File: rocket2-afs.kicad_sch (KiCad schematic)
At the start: 68 parts, among them J1 ARMING_PLUG, J2 POWER, J3 E-MATCH_DROGUE, J4 SWD, J5 E-MATCH_RECOVERY, Q1 Q_NMOS_GSD, Q2 Q_NMOS_GSD, Q3 Q_NMOS_GSD, Q4 Q_NMOS_GSD, Q5 Q_NMOS_GSD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

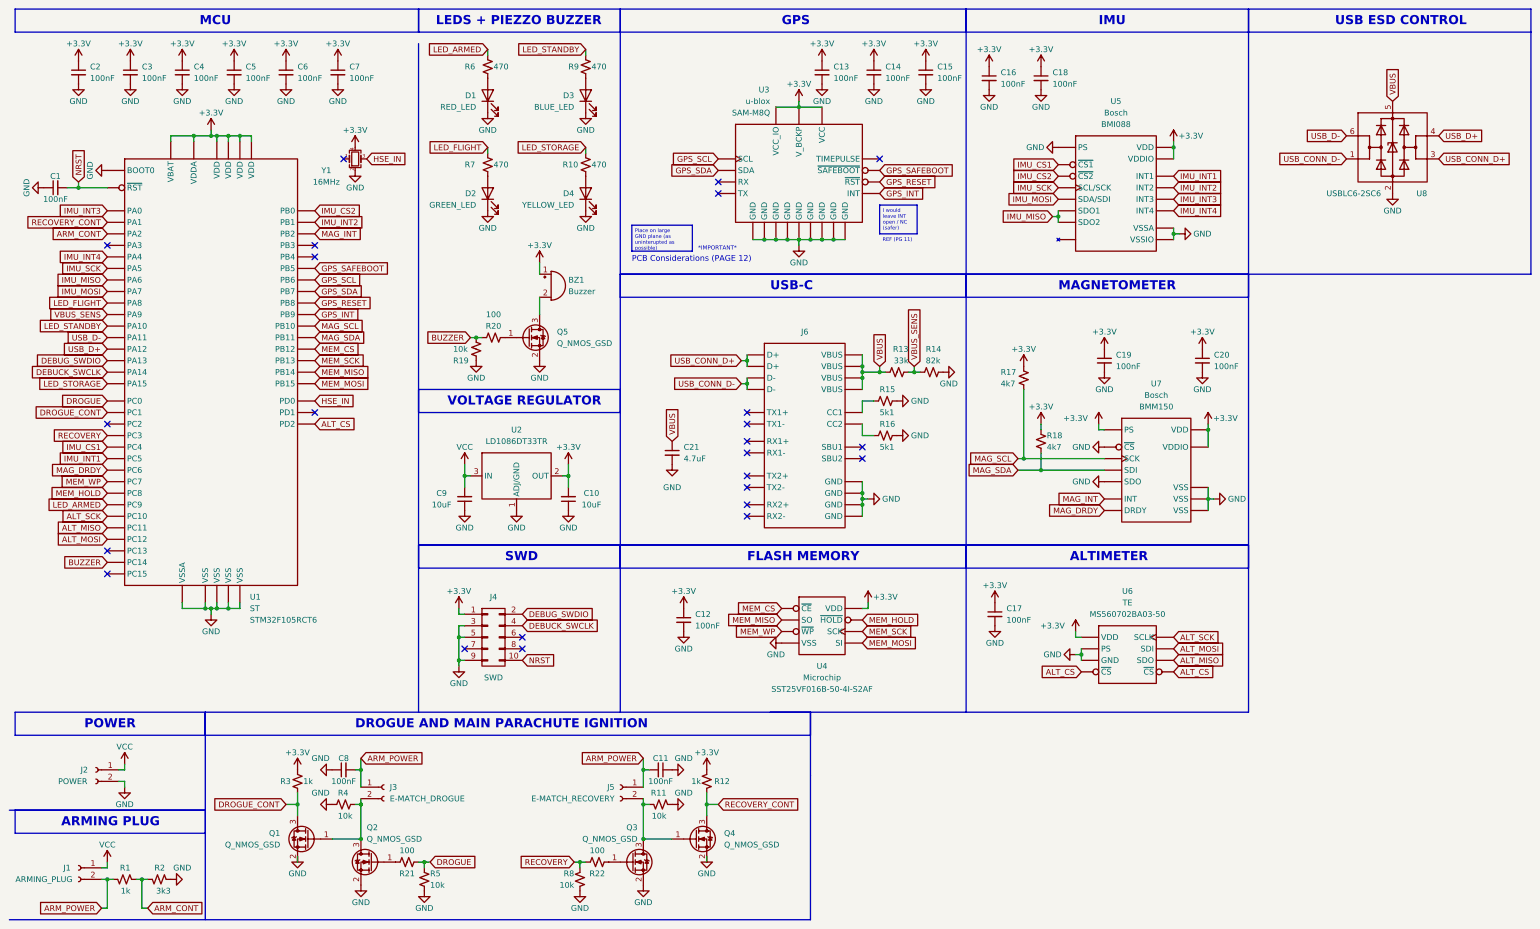
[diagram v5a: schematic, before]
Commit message: Changed Debug Symbol to UCIRP-L Library footrpint
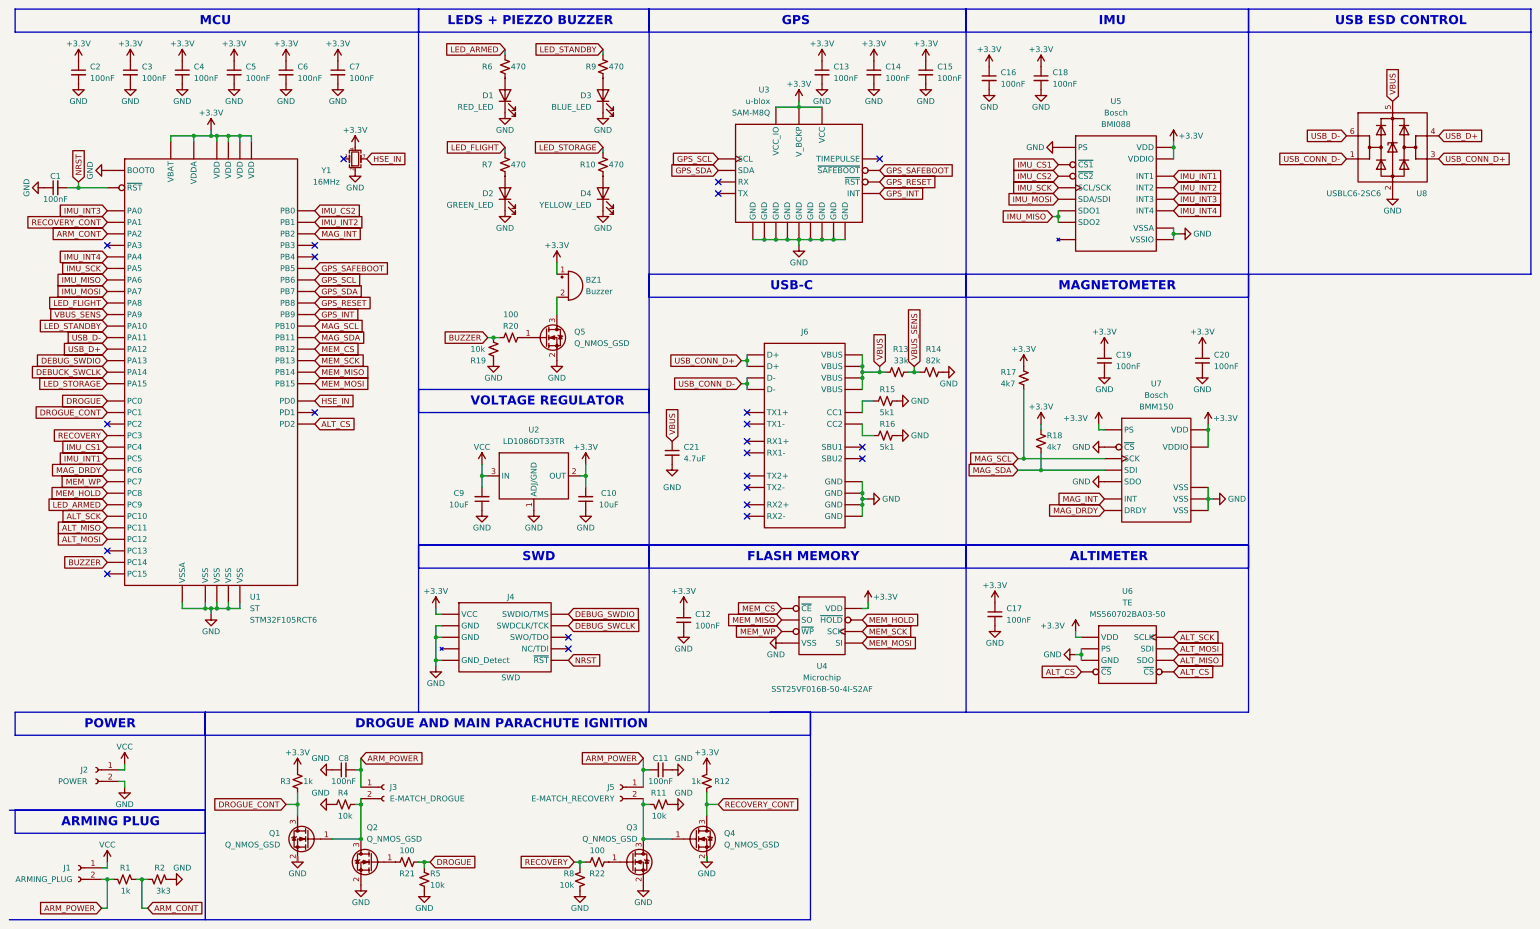
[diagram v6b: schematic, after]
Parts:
- J4: symbol Connector_Generic:Conn_02x05_Odd_Even -> UCIRP-KiCAD-Lib:ARM_Cortex_Debug
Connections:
- net DEBUCK_SWCLK: no longer J4.4 (Pin_4)
- new net DEBUG_SWCLK: J4.4 (SWDCLK/TCK)
- no-connect marks 24 -> 23
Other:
- note removed: "*IMPORTANT*"
- note removed: "PCB Considerations (PAGE 12)"
- note removed: "REF (PG 11)"
- moved on the sheet: BZ1, C10, C9, D1, D2, D3, D4, Q5, R10, R19, R20, R6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

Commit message: Final tweaks
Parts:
- C1, C11, C12, C13, C14, C15, C16, C17, C18, C19, C2, C20, C3, C4, C5, C6, C7, C8: Part # Generic 0603 6.3V 100nF X7R MLCC Capacitor -> Generic 0603 6.3V 100nF X7R MLCC
- C10, C9: Part # Generic 0603 6.3V 10uF X7R MLCC Capacitor -> Generic 0603 6.3V 10uF X7R MLCC
- C21: Part # Generic 0603 6.3V 4.7nF X7R MLCC Capacitor -> Generic 0603 6.3V 4.7uF X7R MLCC
- J4: Part # Generic 2x05 P1.27mm Vertical SMD -> Generic 2x05 P1.27mm Vertical Pin Header SMD
- U4: Manufacturer Microchip -> Winbond; Part # SST25VF016B-50-4I-S2AF -> W25Q128JVSIQ
- Y1: Manufacturer RoHS -> ECS; Part # ECS-1633 -> ECS-1633-160-BN-TR
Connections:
- net DEBUCK_SWCLK is gone; now on net DEBUG_SWCLK: U1.49 (PA14)
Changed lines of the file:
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@@
     )
   )
-  (global_label "DEBUCK_SWCLK" (shape input) (at 33.02 92.71 180) (fields_autoplaced)
+  (global_label "DEBUG_SWCLK" (shape input) (at 33.02 92.71 180) (fields_autoplaced)
     (effects (font (size 1.27 1.27)) (justify right))
-    (property "Intersheetrefs" "${INTERSHEET_REFS}" (at 15.2787 92.71 0)
+    (property "Intersheetrefs" "${INTERSHEET_REFS}" (at 16.5487 92.71 0)
       (effects (font (size 1.27 1.27)) (justify right) hide)
     )
@@
       (effects (font (size 1.27 1.27)) hide)
     )
-    (property "Part #" "Generic 0603 6.3V 100nF X7R MLCC Capacitor" (at 274.32 90.17 0)
+    (property "Part #" "Generic 0603 6.3V 100nF X7R MLCC" (at 274.32 90.17 0)
       (effects (font (size 1.27 1.27)) hide)
     )
@@
       (effects (font (size 1.27 1.27)) hide)
     )
-    (property "Part #" "Generic 0603 6.3V 100nF X7R MLCC Capacitor" (at 38.1 26.67 0)
+    (property "Part #" "Generic 0603 6.3V 100nF X7R MLCC" (at 38.1 26.67 0)
       (effects (font (size 1.27 1.27)) hide)
     )
@@
       (effects (font (size 1.27 1.27)) hide)
     )
-    (property "Part #" "Generic 0603 6.3V 100nF X7R MLCC Capacitor" (at 154.94 180.34 0)
+    (property "Part #" "Generic 0603 6.3V 100nF X7R MLCC" (at 154.94 180.34 0)
       (effects (font (size 1.27 1.27)) hide)
     )
@@
       (effects (font (size 1.27 1.27)) hide)
     )
-    (property "Part #" "Generic 0603 6.3V 10uF X7R MLCC Capacitor" (at 138.43 120.65 0)
+    (property "Part #" "Generic 0603 6.3V 10uF X7R MLCC" (at 138.43 120.65 0)
       (effects (font (size 1.27 1.27)) hide)
     )
@@
       (effects (font (size 1.27 1.27)) hide)
     )
-    (property "Part #" "Generic 0603 6.3V 100nF X7R MLCC Capacitor" (at 72.39 26.67 0)
+    (property "Part #" "Generic 0603 6.3V 100nF X7R MLCC" (at 72.39 26.67 0)
       (effects (font (size 1.27 1.27)) hide)
     )
@@
       (effects (font (size 1.27 1.27)) hide)
     )
-    (property "Part #" "Generic 0603 6.3V 100nF X7R MLCC Capacitor" (at 160.02 147.32 0)
+    (property "Part #" "Generic 0603 6.3V 100nF X7R MLCC" (at 160.02 147.32 0)
       (effects (font (size 1.27 1.27)) hide)
     )
@@
       (effects (font (size 1.27 1.27)) hide)
     )
-    (property "Part #" "Generic 0603 6.3V 100nF X7R MLCC Capacitor" (at 85.09 180.34 0)
+    (property "Part #" "Generic 0603 6.3V 100nF X7R MLCC" (at 85.09 180.34 0)
       (effects (font (size 1.27 1.27)) hide)
     )
@@
       (effects (font (size 1.27 1.27)) hide)
     )
-    (property "Manufacturer" "RoHS" (at 87.63 45.72 0)
+    (property "Manufacturer" "ECS" (at 87.63 45.72 0)
       (effects (font (size 1.27 1.27)) hide)
     )
-    (property "Part #" "ECS-1633" (at 87.63 45.72 0)
+    (property "Part #" "ECS-1633-160-BN-TR" (at 87.63 45.72 0)
       (effects (font (size 1.27 1.27)) hide)
     )
@@
       (effects (font (size 1.27 1.27)) hide)
     )
-    (property "Part #" "Generic 2x05 P1.27mm Vertical SMD" (at 120.65 151.13 0)
+    (property "Part #" "Generic 2x05 P1.27mm Vertical Pin Header SMD" (at 120.65 151.13 0)
       (effects (font (size 1.27 1.27)) hide)
     )
@@
       (effects (font (size 1.27 1.27)) hide)
     )
-    (property "Part #" "Generic 0603 6.3V 100nF X7R MLCC Capacitor" (at 83.82 26.67 0)
+    (property "Part #" "Generic 0603 6.3V 100nF X7R MLCC" (at 83.82 26.67 0)
       (effects (font (size 1.27 1.27)) hide)
     )
@@
       (effects (font (size 1.27 1.27)) hide)
     )
-    (property "Part #" "Generic 0603 6.3V 100nF X7R MLCC Capacitor" (at 213.36 26.67 0)
+    (property "Part #" "Generic 0603 6.3V 100nF X7R MLCC" (at 213.36 26.67 0)
       (effects (font (size 1.27 1.27)) hide)
     )
@@
       (effects (font (size 1.27 1.27)) hide)
     )
-    (property "Part #" "Generic 0603 6.3V 100nF X7R MLCC Capacitor" (at 60.96 26.67 0)
+    (property "Part #" "Generic 0603 6.3V 100nF X7R MLCC" (at 60.96 26.67 0)
       (effects (font (size 1.27 1.27)) hide)
     )
@@
       (effects (font (size 1.27 1.27)) hide)
     )
-    (property "Part #" "Generic 0603 6.3V 100nF X7R MLCC Capacitor" (at 49.53 26.67 0)
+    (property "Part #" "Generic 0603 6.3V 100nF X7R MLCC" (at 49.53 26.67 0)
       (effects (font (size 1.27 1.27)) hide)
     )
@@
       (effects (font (size 1.27 1.27)) hide)
     )
-    (property "Part #" "Generic 0603 6.3V 100nF X7R MLCC Capacitor" (at 21.59 52.07 0)
+    (property "Part #" "Generic 0603 6.3V 100nF X7R MLCC" (at 21.59 52.07 0)
       (effects (font (size 1.27 1.27)) hide)
     )
@@
       (effects (font (size 1.27 1.27)) hide)
     )
-    (property "Part #" "Generic 0603 6.3V 100nF X7R MLCC Capacitor" (at 252.73 90.17 0)
+    (property "Part #" "Generic 0603 6.3V 100nF X7R MLCC" (at 252.73 90.17 0)
       (effects (font (size 1.27 1.27)) hide)
     )
@@
       (effects (font (size 1.27 1.27)) hide)
     )
-    (property "Part #" "Generic 0603 6.3V 10uF X7R MLCC Capacitor" (at 115.57 120.65 0)
+    (property "Part #" "Generic 0603 6.3V 10uF X7R MLCC" (at 115.57 120.65 0)
       (effects (font (size 1.27 1.27)) hide)
     )
@@
       (effects (font (size 1.27 1.27)) hide)
     )
-    (property "Part #" "Generic 0603 6.3V 100nF X7R MLCC Capacitor" (at 238.76 27.94 0)
+    (property "Part #" "Generic 0603 6.3V 100nF X7R MLCC" (at 238.76 27.94 0)
       (effects (font (size 1.27 1.27)) hide)
     )
@@
       (effects (font (size 1.27 1.27)) hide)
     )
-    (property "Part #" "Generic 0603 6.3V 4.7nF X7R MLCC Capacitor" (at 157.48 110.49 0)
+    (property "Part #" "Generic 0603 6.3V 4.7uF X7R MLCC" (at 157.48 110.49 0)
       (effects (font (size 1.27 1.27)) hide)
     )
@@
       (effects (font (size 1.27 1.27)) hide)
     )
-    (property "Part #" "Generic 0603 6.3V 100nF X7R MLCC Capacitor" (at 190.5 26.67 0)
+    (property "Part #" "Generic 0603 6.3V 100nF X7R MLCC" (at 190.5 26.67 0)
       (effects (font (size 1.27 1.27)) hide)
     )
@@
       (effects (font (size 1.27 1.27)) hide)
     )
-    (property "Datasheet" "https://ww1.microchip.com/downloads/en/DeviceDoc/20005044C.pdf" (at 190.5 148.59 0)
+    (property "Datasheet" "https://www.winbond.com/resource-files/W25Q128JV%20RevI%2008232021%20Plus.pdf" (at 190.5 148.59 0)
       (effects (font (size 1.27 1.27)) hide)
     )
-    (property "Manufacturer" "Microchip" (at 190.5 160.02 0)
+    (property "Manufacturer" "Winbond" (at 190.5 160.02 0)
       (effects (font (size 1.27 1.27)))
     )
-    (property "Part #" "SST25VF016B-50-4I-S2AF" (at 190.5 162.56 0)
+    (property "Part #" "W25Q128JVSIQ" (at 190.5 162.56 0)
       (effects (font (size 1.27 1.27)))
     )
@@
       (effects (font (size 1.27 1.27)) hide)
     )
-    (property "Part #" "Generic 0603 6.3V 100nF X7R MLCC Capacitor" (at 228.6 146.05 0)
+    (property "Part #" "Generic 0603 6.3V 100nF X7R MLCC" (at 228.6 146.05 0)
       (effects (font (size 1.27 1.27)) hide)
     )
@@
       (effects (font (size 1.27 1.27)) hide)
     )
-    (property "Datasheet" "https://www.we-online.com/components/products/datasheet/629105150521.pdf" (at 186.69 106.68 0)
+    (property "Datasheet" "https://gct.co/files/drawings/usb4105.pdf?v=5f9eb85e-7d29-4c03-ba83-51194e8d0df3" (at 186.69 106.68 0)
       (effects (font (size 1.27 1.27)) hide)
     )
@@
       (effects (font (size 1.27 1.27)) hide)
     )
-    (property "Part #" "Generic 0603 6.3V 100nF X7R MLCC Capacitor" (at 227.33 27.94 0)
+    (property "Part #" "Generic 0603 6.3V 100nF X7R MLCC" (at 227.33 27.94 0)
       (effects (font (size 1.27 1.27)) hide)
     )
@@
       (effects (font (size 1.27 1.27)) hide)
     )
-    (property "Part #" "Generic 0603 6.3V 100nF X7R MLCC Capacitor" (at 201.93 26.67 0)
+    (property "Part #" "Generic 0603 6.3V 100nF X7R MLCC" (at 201.93 26.67 0)
       (effects (font (size 1.27 1.27)) hide)
     )
@@
       (effects (font (size 1.27 1.27)) hide)
     )
-    (property "Part #" "Generic 0603 6.3V 100nF X7R MLCC Capacitor" (at 26.67 26.67 0)
+    (property "Part #" "Generic 0603 6.3V 100nF X7R MLCC" (at 26.67 26.67 0)
       (effects (font (size 1.27 1.27)) hide)
     )

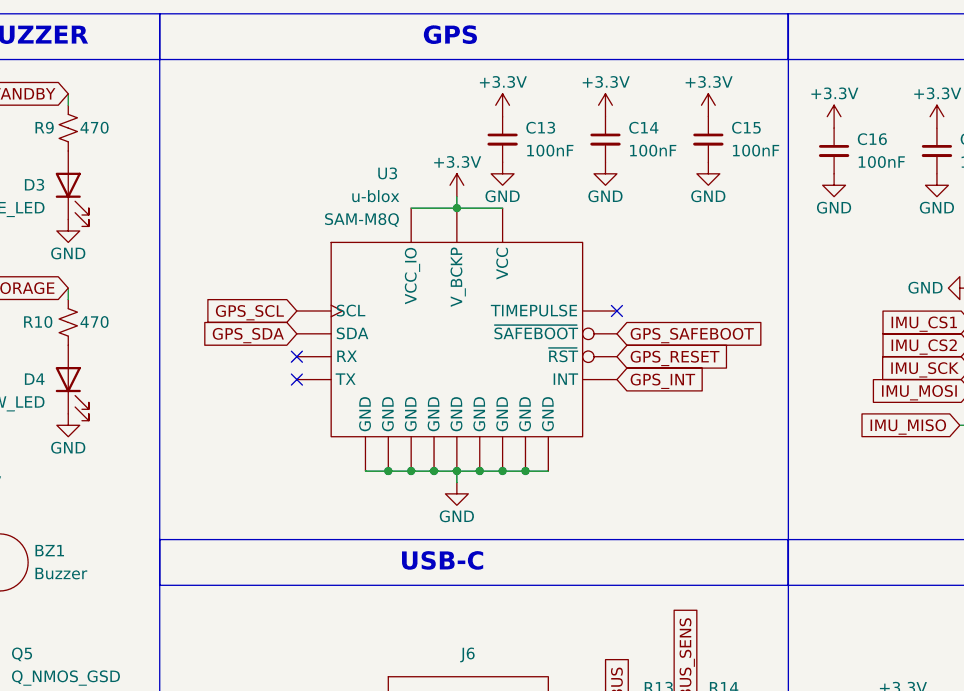
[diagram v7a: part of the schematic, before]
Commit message: Added GPS RESET pullup resistor to PCB
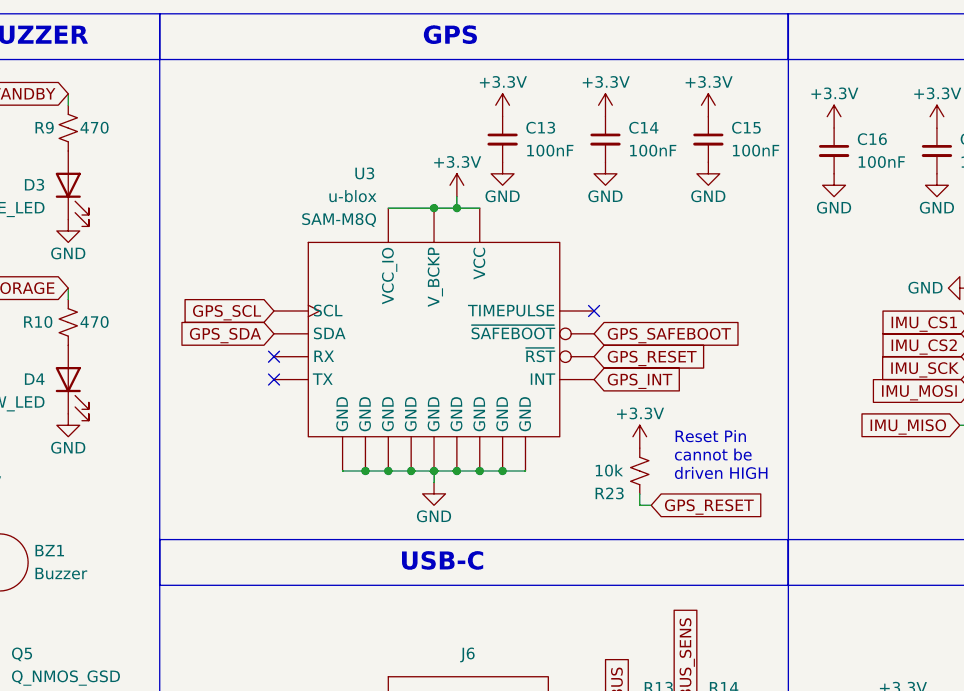
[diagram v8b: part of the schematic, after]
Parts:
- added R23: 10k, Resistor_SMD:R_0603_1608Metric, symbol Device:R_Small_US
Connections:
- net +3.3V: now also R23.1
- net GPS_RESET: now also R23.2
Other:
- note added: "Reset Pin cannot be driven HIGH"
- moved on the sheet: U3
